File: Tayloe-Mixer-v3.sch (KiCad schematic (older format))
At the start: 42 parts, among them J1 BNC, J2 Pad, J3 Audio_Jack, J4 Conn_01x04_Female, J5 Pad, T1 6:31, T2 31:6, T3 T50_SPLITTER, U2 FST3253, U3 LM358, U4 si5351, U6 MMG3

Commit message: added esp32
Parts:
- removed J3: Audio_Jack, Xenir:Audio_Jack, symbol Tayloe-Mixer-v2-rescue:Audio_Jack-Xenir
- removed J4: Conn_01x04_Female, Connector_PinHeader_2.54mm:PinHeader_1x04_P2.54mm_Vertical, symbol Connector:Conn_01x04_Female
- removed U?: ESP32-A1S, symbol xenir:ESP32-A1S
- added C1, C2: .1uF, symbol xenir:Capacitor
- added C3, C4: 1uF, symbol xenir:Capacitor
- added C5, C6: 22uF, symbol xenir:Cap_Polarized
- added D1: LCD_I2C, symbol xenir:LCD_I2C
- added J1: Audio_Jack, symbol xenir:Audio_Jack
- added Q1, Q2: 2N3904, Package_TO_SOT_THT:TO-92_Inline, symbol Transistor_BJT:2N3904
- added R1, R2: Resistor, symbol esp32-a1s-rescue:Resistor-Xenir
- added R3, R4: 330, symbol xenir:Resistor
- added SW1: SW_DIP_x01, symbol Switch:SW_DIP_x01
- added SW2: Rotary_Encoder_Switch, symbol Device:Rotary_Encoder_Switch
- added U1: ESP32-A1S, symbol xenir:ESP32-A1S
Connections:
- net labels added: DTR, EN, IO0, I_SIGNAL, OUTL, OUTR, Q_SIGNAL, RTS, RX0, SCL, SDA, TX0
- net labels removed: I_OUTPUT, Q_OUTPUT
- wire segments 166 -> 211
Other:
- moved on the sheet: C1, C10, C11, C12, C13, C14, C15, C16, C2, C25, C3, C4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

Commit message: annotate
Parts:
- C101: renamed from C1; footprint (none) -> xenir:Capacitor 1206
- C102: renamed from C2; footprint (none) -> xenir:Capacitor 1206
- C103: renamed from C3; footprint (none) -> xenir:Capacitor 1206
- C104: renamed from C4; footprint (none) -> xenir:Capacitor 1206
- C105: renamed from C5; footprint (none) -> xenir:Cap_4x5.4
- C106: renamed from C6; footprint (none) -> xenir:Cap_4x5.4
- D1: footprint (none) -> xenir:LCD_I2C
- J101: renamed from J1; footprint (none) -> xenir:Audio_Jack
- R101: renamed from R1; footprint (none) -> xenir:Resistor 0805
- R102: renamed from R2; footprint (none) -> xenir:Resistor 0805
- R103: renamed from R3; footprint (none) -> xenir:Resistor 0805
- R104: renamed from R4; footprint (none) -> xenir:Resistor 0805
- U1: footprint (none) -> xenir:ESP32-A1S
- U3: value LM358 -> LM4562
- gave numbers to parts that had none: 2
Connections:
- wire segments 211 -> 199
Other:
- moved on the sheet: C101, C102, C103, C104, C105, C106, D1, J101, R101, R102, R103, R104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

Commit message: gg
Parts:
- removed Q1, Q2: 2N3904, Package_TO_SOT_THT:TO-92_Inline, symbol Transistor_BJT:2N3904
- removed R101, R102: Resistor, xenir:Resistor 0805, symbol esp32-a1s-rescue:Resistor-Xenir
- added Q? (x2): 2N3904-SMD, Package_TO_SOT_SMD:SOT-23, symbol xenir:2N3904-SMD
- added R? (x2): 10k, xenir:Resistor 0805, symbol esp32-a1s-rescue:Resistor-Xenir
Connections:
- net labels added: IO
- wire segments 199 -> 200
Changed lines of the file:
@@
 Wire Wire Line
 	6700 7100 6850 7100
-$Comp
-L Transistor_BJT:2N3904 Q1
-U 1 1 6287DEE6
-P 3925 6025
-F 0 "Q1" H 4115 6071 50  0000 L CNN
-F 1 "2N3904" H 4115 5980 50  0000 L CNN
-F 2 "Package_TO_SOT_THT:TO-92_Inline" H 4125 5950 50  0001 L CIN
-F 3 "https://www.onsemi.com/pub/Collateral/2N3903-D.PDF" H 3925 6025 50  0001 L CNN
-	1    3925 6025
-	1    0    0    -1
-$EndComp
-$Comp
-L Transistor_BJT:2N3904 Q2
-U 1 1 6287F786
-P 3925 6850
-F 0 "Q2" H 4115 6804 50  0000 L CNN
-F 1 "2N3904" H 4115 6895 50  0000 L CNN
-F 2 "Package_TO_SOT_THT:TO-92_Inline" H 4125 6775 50  0001 L CIN
-F 3 "https://www.onsemi.com/pub/Collateral/2N3903-D.PDF" H 3925 6850 50  0001 L CNN
-	1    3925 6850
-	1    0    0    1
-$EndComp
-Text GLabel 3225 6025 0    50   Input ~ 0
-DTR
-Text GLabel 3225 6850 0    50   Input ~ 0
-RTS
-$Comp
-L esp32-a1s-rescue:Resistor-Xenir R101
-U 1 1 62884B2D
-P 3525 6025
-F 0 "R101" H 3525 6179 28  0000 C CNN
-F 1 "Resistor" H 3525 6122 28  0000 C CNN
-F 2 "xenir:Resistor 0805" H 3525 5925 50  0001 C CNN
-F 3 "" H 3525 5925 50  0001 C CNN
-	1    3525 6025
-	1    0    0    -1
-$EndComp
-$Comp
-L esp32-a1s-rescue:Resistor-Xenir R102
-U 1 1 628852B4
-P 3525 6850
-F 0 "R102" H 3525 7004 28  0000 C CNN
-F 1 "Resistor" H 3525 6947 28  0000 C CNN
-F 2 "xenir:Resistor 0805" H 3525 6750 50  0001 C CNN
-F 3 "" H 3525 6750 50  0001 C CNN
-	1    3525 6850
-	1    0    0    -1
-$EndComp
-Wire Wire Line
-	3225 6025 3325 6025
-Wire Wire Line
-	3225 6850 3275 6850
-Wire Wire Line
-	4025 6225 4025 6350
-Wire Wire Line
-	4025 6350 3275 6350
-Wire Wire Line
-	3275 6350 3275 6850
-Connection ~ 3275 6850
-Wire Wire Line
-	3275 6850 3325 6850
-Wire Wire Line
-	3325 6025 3325 6500
-Wire Wire Line
-	3325 6500 4025 6500
-Wire Wire Line
-	4025 6500 4025 6650
-Connection ~ 3325 6025
-Wire Wire Line
-	4025 5825 4025 5650
-Wire Wire Line
-	4025 5650 4250 5650
-Wire Wire Line
-	4025 7050 4025 7225
-Wire Wire Line
-	4025 7225 4275 7225
-Text GLabel 4250 5650 2    50   Input ~ 0
+Text GLabel 3950 4750 2    50   Input ~ 0
 EN
-Text GLabel 4275 7225 2    50   Input ~ 0
+Text GLabel 4125 7025 2    50   Input ~ 0
 IO0
 $Comp
@@
 Text GLabel 6600 8050 2    50   Input ~ 0
 SDA
+$Comp
+L xenir:2N3904-SMD Q?
+U 1 1 63749133
+P 3600 5050
+F 0 "Q?" H 3691 4946 50  0000 L CNN
+F 1 "2N3904-SMD" H 3691 4855 50  0000 L CNN
+F 2 "Package_TO_SOT_SMD:SOT-23" H 3700 4825 50  0001 L CIN
+F 3 "https://www.fairchildsemi.com/datasheets/2N/2N3904.pdf" H 3500 4900 50  0001 L CNN
+	1    3600 5050
+	1    0    0    -1
+$EndComp
+Wire Wire Line
+	3600 5000 3600 4750
+Wire Wire Line
+	3600 4750 3950 4750
+$Comp
+L esp32-a1s-rescue:Resistor-Xenir R?
+U 1 1 637D5201
+P 3100 5200
+F 0 "R?" H 3100 5354 28  0000 C CNN
+F 1 "10k" H 3100 5297 28  0000 C CNN
+F 2 "xenir:Resistor 0805" H 3100 5100 50  0001 C CNN
+F 3 "" H 3100 5100 50  0001 C CNN
+	1    3100 5200
+	1    0    0    -1
+$EndComp
+Text GLabel 2750 5200 0    50   Input ~ 0
+DTR
+Wire Wire Line
+	2750 5200 2850 5200
+$Comp
+L esp32-a1s-rescue:Resistor-Xenir R?
+U 1 1 63814A82
+P 3100 5950
+F 0 "R?" H 3100 6104 28  0000 C CNN
+F 1 "10k" H 3100 6047 28  0000 C CNN
+F 2 "xenir:Resistor 0805" H 3100 5850 50  0001 C CNN
+F 3 "" H 3100 5850 50  0001 C CNN
+	1    3100 5950
+	1    0    0    -1
+$EndComp
+Text GLabel 2750 5950 0    50   Input ~ 0
+RTS
+Wire Wire Line
+	2750 5950 2800 5950
+$Comp
+L xenir:2N3904-SMD Q?
+U 1 1 63824306
+P 3600 6100
+F 0 "Q?" H 3691 5904 50  0000 L CNN
+F 1 "2N3904-SMD" H 3691 5995 50  0000 L CNN
+F 2 "Package_TO_SOT_SMD:SOT-23" H 3700 5875 50  0001 L CIN
+F 3 "https://www.fairchildsemi.com/datasheets/2N/2N3904.pdf" H 3500 5950 50  0001 L CNN
+	1    3600 6100
+	1    0    0    1
+$EndComp
+Wire Wire Line
+	2850 5550 3600 5550
+Wire Wire Line
+	3600 5550 3600 5750
+Wire Wire Line
+	2850 5200 2850 5550
+Connection ~ 2850 5200
+Wire Wire Line
+	2850 5200 2900 5200
+Wire Wire Line
+	2800 5950 2800 5500
+Wire Wire Line
+	2800 5500 3600 5500
+Wire Wire Line
+	3600 5500 3600 5400
+Connection ~ 2800 5950
+Wire Wire Line
+	2800 5950 2900 5950
+Text GLabel 3950 6400 2    50   Input ~ 0
+IO
+Wire Wire Line
+	3600 6400 3950 6400
+Wire Wire Line
+	3600 6150 3600 6400
 $EndSCHEMATC

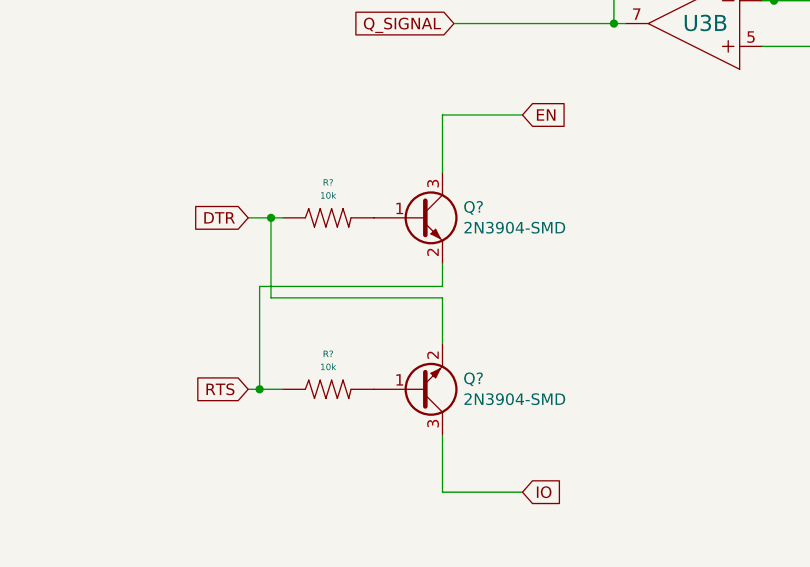
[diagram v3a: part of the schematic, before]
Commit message: finished footprints
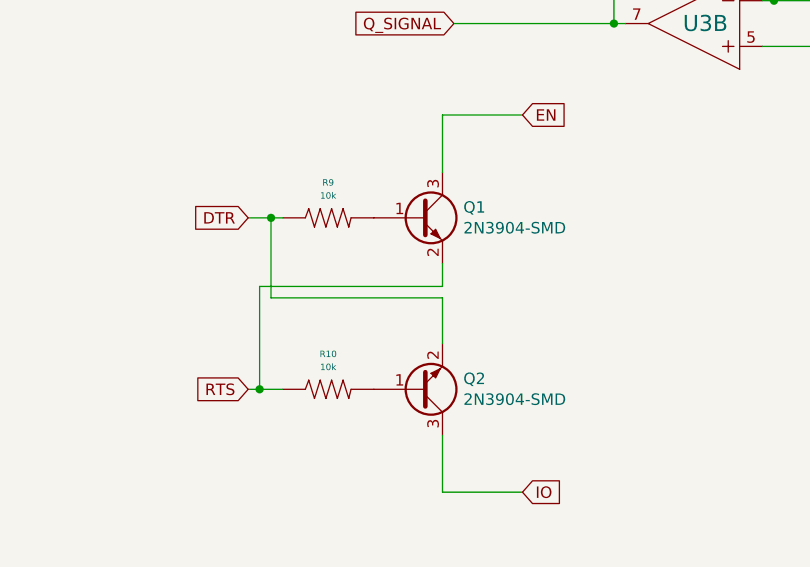
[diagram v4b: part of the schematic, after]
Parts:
- SW1: footprint (none) -> Button_Switch_THT:SW_PUSH_6mm
- SW2: footprint (none) -> Rotary_Encoder:RotaryEncoder_Alps_EC11E-Switch_Vertical_H20mm
- gave numbers to parts that had none: 4
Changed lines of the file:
@@
 F 0 "SW2" H 3750 7983 50  0000 C CNN
 F 1 "Rotary_Encoder_Switch" H 3750 8074 50  0000 C CNN
-F 2 "" H 3600 8510 50  0001 C CNN
+F 2 "Rotary_Encoder:RotaryEncoder_Alps_EC11E-Switch_Vertical_H20mm" H 3600 8510 50  0001 C CNN
 F 3 "~" H 3750 8610 50  0001 C CNN
 	1    3750 8350
@@
 F 0 "SW1" H 3500 7667 50  0000 C CNN
 F 1 "SW_DIP_x01" H 3500 7576 50  0000 C CNN
-F 2 "" H 3500 7400 50  0001 C CNN
+F 2 "Button_Switch_THT:SW_PUSH_6mm" H 3500 7400 50  0001 C CNN
 F 3 "~" H 3500 7400 50  0001 C CNN
 	1    3500 7400
@@
 SDA
 $Comp
-L xenir:2N3904-SMD Q?
+L xenir:2N3904-SMD Q1
 U 1 1 63749133
 P 3600 5050
-F 0 "Q?" H 3691 4946 50  0000 L CNN
+F 0 "Q1" H 3691 4946 50  0000 L CNN
 F 1 "2N3904-SMD" H 3691 4855 50  0000 L CNN
 F 2 "Package_TO_SOT_SMD:SOT-23" H 3700 4825 50  0001 L CIN
@@
 	3600 4750 3950 4750
 $Comp
-L esp32-a1s-rescue:Resistor-Xenir R?
+L esp32-a1s-rescue:Resistor-Xenir R9
 U 1 1 637D5201
 P 3100 5200
-F 0 "R?" H 3100 5354 28  0000 C CNN
+F 0 "R9" H 3100 5354 28  0000 C CNN
 F 1 "10k" H 3100 5297 28  0000 C CNN
 F 2 "xenir:Resistor 0805" H 3100 5100 50  0001 C CNN
@@
 	2750 5200 2850 5200
 $Comp
-L esp32-a1s-rescue:Resistor-Xenir R?
+L esp32-a1s-rescue:Resistor-Xenir R10
 U 1 1 63814A82
 P 3100 5950
-F 0 "R?" H 3100 6104 28  0000 C CNN
+F 0 "R10" H 3100 6104 28  0000 C CNN
 F 1 "10k" H 3100 6047 28  0000 C CNN
 F 2 "xenir:Resistor 0805" H 3100 5850 50  0001 C CNN
@@
 	2750 5950 2800 5950
 $Comp
-L xenir:2N3904-SMD Q?
+L xenir:2N3904-SMD Q2
 U 1 1 63824306
 P 3600 6100
-F 0 "Q?" H 3691 5904 50  0000 L CNN
+F 0 "Q2" H 3691 5904 50  0000 L CNN
 F 1 "2N3904-SMD" H 3691 5995 50  0000 L CNN
 F 2 "Package_TO_SOT_SMD:SOT-23" H 3700 5875 50  0001 L CIN

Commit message: updated pcb
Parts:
- removed J5: Pad, Xenir:Pad, symbol Tayloe-Mixer-v2-rescue:Pad-Xenir
- removed U6: MMG3, Package_TO_SOT_SMD:SOT-89-3_Handsoldering, symbol xenir:MMG3
- added C203: .1uF, xenir:Capacitor 1206, symbol preamp-mar6-rescue:Capacitor-xenir
- added C204: 10uF, xenir:Cap_4x5.4, symbol preamp-mar6-rescue:Cap_Polarized-xenir
- added J3: Jack-DC, Connector_BarrelJack:BarrelJack_Horizontal, symbol Connector:Jack-DC
- added L201: T37-43 10T, xenir:T37_Inductor, symbol preamp-mar6-rescue:Inductor-xenir
- added R201: 536, xenir:Resistor 1206, symbol preamp-mar6-rescue:Resistor-xenir
- added U201: MAR6, xenir:VV105, symbol preamp-mar6-rescue:MAR6-xenir
- renumbered C1 to C201, C16 to C202
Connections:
- net +12V: now also C203.1, C204.1, J3.1, R201.1
- net GND: now also C203.2, C204.2, J3.2, U201.2 (GND), U201.4 (GND)
- net at C201.2: now also U201.1
- net at C202.1: now also L201.2, U201.3
- new net: L201.1, R201.2
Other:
- moved on the sheet: C10, C101, C102, C103, C104, C105, C106, C11, C12, C13, C14, C15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

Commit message: continue
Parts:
- added J4: Conn_01x07_Female, Connector_PinSocket_2.54mm:PinSocket_1x07_P2.54mm_Vertical, symbol Connector:Conn_01x07_Female
- U7: footprint Package_TO_SOT_SMD:TO-252-3_TabPin2 -> Package_TO_SOT_SMD:SOT-223-3_TabPin2
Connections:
- net IO is gone; now on net IO0: Q2.3 (C)
- net DTR: now also J4.1 (Pin_1)
- net GND: now also J4.6 (Pin_6)
- net RTS: now also J4.7 (Pin_7)
- net RX0: now also J4.3 (Pin_3)
- net TX0: now also J4.2 (Pin_2)
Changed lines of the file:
@@
 F 0 "U7" H 10550 1892 50  0000 C CNN
 F 1 "AMS1117CD-3.3" H 10550 1801 50  0000 C CNN
-F 2 "Package_TO_SOT_SMD:TO-252-3_TabPin2" H 10550 1850 50  0001 C CNN
+F 2 "Package_TO_SOT_SMD:SOT-223-3_TabPin2" H 10550 1850 50  0001 C CNN
 F 3 "http://www.advanced-monolithic.com/pdf/ds1117.pdf" H 10650 1400 50  0001 C CNN
 	1    10550 1650
@@
 Text GLabel 2600 7450 2    50   Input ~ 0
 EN
-Text GLabel 4275 7225 2    50   Input ~ 0
-IO0
 $Comp
 L Switch:SW_DIP_x01 SW1
@@
 	1450 8650 1550 8650
 Text GLabel 2600 9100 2    50   Input ~ 0
-IO
+IO0
 Wire Wire Line
 	2250 9100 2600 9100
@@
 Wire Wire Line
 	7050 1200 7050 1400
+$Comp
+L Connector:Conn_01x07_Female J4
+U 1 1 634014D2
+P 1300 6900
+F 0 "J4" H 1192 6375 50  0000 C CNN
+F 1 "Conn_01x07_Female" H 1192 6466 50  0000 C CNN
+F 2 "Connector_PinSocket_2.54mm:PinSocket_1x07_P2.54mm_Vertical" H 1300 6900 50  0001 C CNN
+F 3 "~" H 1300 6900 50  0001 C CNN
+	1    1300 6900
+	-1   0    0    1
+$EndComp
+Text GLabel 1500 7200 2    50   Input ~ 0
+DTR
+Text GLabel 1500 7100 2    50   Input ~ 0
+TX0
+Text GLabel 1500 7000 2    50   Input ~ 0
+RX0
+$Comp
+L power:GND #PWR0127
+U 1 1 63404260
+P 1650 6700
+F 0 "#PWR0127" H 1650 6450 50  0001 C CNN
+F 1 "GND" H 1655 6527 50  0000 C CNN
+F 2 "" H 1650 6700 50  0001 C CNN
+F 3 "" H 1650 6700 50  0001 C CNN
+	1    1650 6700
+	1    0    0    -1
+$EndComp
+Wire Wire Line
+	1500 6700 1650 6700
+Text GLabel 1500 6600 2    50   Input ~ 0
+RTS
 $EndSCHEMATC

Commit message: board
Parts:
- removed J2: Pad, Xenir:Pad, symbol Tayloe-Mixer-v2-rescue:Pad-Xenir
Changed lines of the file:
@@
 	1    0    0    -1
 $EndComp
-$Comp
-L Tayloe-Mixer-v2-rescue:Pad-Xenir J2
-U 1 1 5F4876B8
-P 9200 2700
-F 0 "J2" H 9100 2550 50  0000 C CNN
-F 1 "Pad" H 9200 2450 50  0000 C CNN
-F 2 "Xenir:Pad" H 9200 2700 50  0001 C CNN
-F 3 "" H 9200 2700 50  0001 C CNN
-	1    9200 2700
-	1    0    0    -1
-$EndComp
-Connection ~ 9300 2850
 $Bitmap
 Pos 33350 13700
